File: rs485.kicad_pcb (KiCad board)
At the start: 2 copper layers, 4 parts, among them J1 Conn_01x12_Pin, J3 Conn_01x12_Pin, U2 SN74CB3Q3384APW

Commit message: pcb
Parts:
- moved U2 10.0 mm to (147.3, 92.5)
- moved U1 5.28 mm to (147.4, 82.2)
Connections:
- J1 pad 10: VCC -> Net-(J1-Pin_10)
- J1 pad 12: Net-(J1-Pin_12) -> VCC
- U1 pad 6: Net-(J1-Pin_11) -> Net-(J1-Pin_10)
- U1 pad 7: Net-(J1-Pin_12) -> Net-(J1-Pin_11)
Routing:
- net VCC: track 0.00 -> 30.4 mm
- net Net-(J1-Pin_6): track 0.00 -> 26.7 mm, vias 0 -> 2
- net Net-(J3-Pin_10): track 0.00 -> 22.2 mm, vias 0 -> 2
- net Net-(J3-Pin_12): track 0.00 -> 21.9 mm
- net Net-(J3-Pin_11): track 0.00 -> 20.3 mm, vias 0 -> 2
- net Net-(J1-Pin_1): track 0.00 -> 18.9 mm
- net Net-(J1-Pin_11): track 0.00 -> 18.5 mm
- net Net-(J1-Pin_10): track 0.00 -> 18.0 mm
- net Net-(J1-Pin_5): track 0.00 -> 17.6 mm, vias 0 -> 1
- net GND: track 0.00 -> 17.4 mm
- net Net-(J1-Pin_2): track 0.00 -> 17.0 mm, vias 0 -> 2
- net Net-(J1-Pin_3): track 0.00 -> 16.5 mm, vias 0 -> 2
- net Net-(U1-D): track 0.00 -> 16.3 mm
- net Net-(J1-Pin_4): track 0.00 -> 16.0 mm, vias 0 -> 1
- net Net-(U1-DE): track 0.00 -> 10.4 mm
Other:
- board outline added: 46.2 x 39.9 mm

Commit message: pcb ok.
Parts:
- moved J3 26.5 mm to (133.6, 97.3)
- moved U2 26.2 mm to (150.3, 118.5), turned to 180 degrees
- moved J1 26.2 mm to (165.6, 125.2)
- moved U1 25.7 mm to (150.6, 107.7)
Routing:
- net VCC: track 30.4 -> 67.2 mm
- net Net-(J3-Pin_1): track 0.00 -> 35.7 mm, vias 0 -> 1
- net Net-(J3-Pin_5): track 0.00 -> 34.4 mm
- net Net-(J3-Pin_2): track 0.00 -> 34.1 mm, vias 0 -> 1
- net Net-(J3-Pin_4): track 0.00 -> 30.2 mm
- net Net-(J3-Pin_3): track 0.00 -> 28.8 mm, vias 0 -> 1
- net Net-(J1-Pin_8): track 0.00 -> 20.8 mm
- net Net-(J3-Pin_6): track 0.00 -> 18.6 mm
- net Net-(J3-Pin_7): track 0.00 -> 15.9 mm
- net Net-(J3-Pin_9): track 0.00 -> 15.6 mm, vias 0 -> 1
- net Net-(J1-Pin_7): track 0.00 -> 15.3 mm
- net Net-(J3-Pin_8): track 0.00 -> 15.1 mm
- net Net-(J3-Pin_12): track 21.9 -> 30.7 mm
- net Net-(J1-Pin_4): track 16.0 -> 24.4 mm, vias 1 -> 0
- net Net-(J3-Pin_10): track 22.2 -> 14.2 mm, vias 2 -> 0
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- added copper zone on B.Cu, net GND
- added copper zone on F.Cu, net GND
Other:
- board size 46.2 x 39.9 mm -> 42.2 x 34.8 mm

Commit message: pcb开始制作了。
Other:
- board text added: "10E"
- board text added: "1A3"
- board text added: "1A4"
- board text added: "1A5"
- board text added: "1B1"
- board text added: "1B2"
- board text added: "1B3"
- board text added: "1B4"
- board text added: "1B5"
- board text added: "20E"
- board text added: "2A1"
- board text added: "2A2"
- board text added: "2A3"
- board text added: "2A4"
- board text added: "2A5"
- board text added: "2B1"
- board text added: "2B2"
- board text added: "2B3"
- board text added: "2B4"
- board text added: "2B5"
- board text added: "A"
- board text added: "B"
- board text added: "GND"
- board text added: "VCC"
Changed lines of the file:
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@@
       (plot_on_all_layers_selection 0x0000000_00000000)
       (disableapertmacros false)
-      (usegerberextensions false)
-      (usegerberattributes true)
-      (usegerberadvancedattributes true)
-      (creategerberjobfile true)
+      (usegerberextensions true)
+      (usegerberattributes false)
+      (usegerberadvancedattributes false)
+      (creategerberjobfile false)
       (dashed_line_dash_ratio 12.000000)
       (dashed_line_gap_ratio 3.000000)
@@
       (plotinvisibletext false)
       (sketchpadsonfab false)
-      (subtractmaskfromsilk false)
+      (subtractmaskfromsilk true)
       (outputformat 1)
       (mirror false)
-      (drillshape 1)
+      (drillshape 0)
       (scaleselection 1)
-      (outputdirectory "")
+      (outputdirectory "irg")
     )
   )
@@
   (gr_rect (start 129.286 93.726) (end 171.45 128.524)
     (stroke (width 0.1) (type default)) (fill none) (layer "Edge.Cuts"))
+  (gr_text "1B1" (at 136.144 97.79) (layer "F.SilkS")
+    (effects (font (size 1 1) (thickness 0.15)) (justify left bottom))
+  )
+  (gr_text "VCC" (at 160.274 97.79) (layer "F.SilkS")
+    (effects (font (size 1 1) (thickness 0.15)) (justify left bottom))
+  )
+  (gr_text "2A5" (at 136.906 120.65) (layer "F.SilkS")
+    (effects (font (size 1 1) (thickness 0.15)) (justify left bottom))
+  )
+  (gr_text "2B3" (at 160.274 120.904) (layer "F.SilkS")
+    (effects (font (size 1 1) (thickness 0.15)) (justify left bottom))
+  )
+  (gr_text "1B5" (at 160.274 113.03) (layer "F.SilkS")
+    (effects (font (size 1 1) (thickness 0.15)) (justify left bottom))
+  )
+  (gr_text "2A2" (at 136.144 113.03) (layer "F.SilkS")
+    (effects (font (size 1 1) (thickness 0.15)) (justify left bottom))
+  )
+  (gr_text "1B2" (at 136.144 100.076) (layer "F.SilkS")
+    (effects (font (size 1 1) (thickness 0.15)) (justify left bottom))
+  )
+  (gr_text "1B4" (at 160.274 110.49) (layer "F.SilkS")
+    (effects (font (size 1 1) (thickness 0.15)) (justify left bottom))
+  )
+  (gr_text "10E" (at 136.144 123.444) (layer "F.SilkS")
+    (effects (font (size 1 1) (thickness 0.15)) (justify left bottom))
+  )
+  (gr_text "1A5" (at 136.144 107.95) (layer "F.SilkS")
+    (effects (font (size 1 1) (thickness 0.15)) (justify left bottom))
+  )
+  (gr_text "2A1" (at 136.144 110.744) (layer "F.SilkS")
+    (effects (font (size 1 1) (thickness 0.15)) (justify left bottom))
+  )
+  (gr_text "B" (at 160.274 102.87) (layer "F.SilkS")
+    (effects (font (size 1 1) (thickness 0.15)) (justify left bottom))
+  )
+  (gr_text "2A4" (at 136.144 118.11) (layer "F.SilkS")
+    (effects (font (size 1 1) (thickness 0.15)) (justify left bottom))
+  )
+  (gr_text "1A3" (at 136.144 102.87) (layer "F.SilkS")
+    (effects (font (size 1 1) (thickness 0.15)) (justify left bottom))
+  )
+  (gr_text "2A3" (at 136.144 115.57) (layer "F.SilkS")
+    (effects (font (size 1 1) (thickness 0.15)) (justify left bottom))
+  )
+  (gr_text "GND" (at 160.274 105.41) (layer "F.SilkS")
+    (effects (font (size 1 1) (thickness 0.15)) (justify left bottom))
+  )
+  (gr_text "1A4" (at 136.144 105.41) (layer "F.SilkS")
+    (effects (font (size 1 1) (thickness 0.15)) (justify left bottom))
+  )
+  (gr_text "20E" (at 136.144 125.73) (layer "F.SilkS")
+    (effects (font (size 1 1) (thickness 0.15)) (justify left bottom))
+  )
+  (gr_text "1B3" (at 160.274 107.95) (layer "F.SilkS")
+    (effects (font (size 1 1) (thickness 0.15)) (justify left bottom))
+  )
+  (gr_text "2B5" (at 160.274 125.984) (layer "F.SilkS")
+    (effects (font (size 1 1) (thickness 0.15)) (justify left bottom))
+  )
+  (gr_text "A" (at 160.274 100.33) (layer "F.SilkS")
+    (effects (font (size 1 1) (thickness 0.15)) (justify left bottom))
+  )
+  (gr_text "2B2" (at 160.274 118.11) (layer "F.SilkS")
+    (effects (font (size 1 1) (thickness 0.15)) (justify left bottom))
+  )
+  (gr_text "2B4" (at 160.274 123.952) (layer "F.SilkS")
+    (effects (font (size 1 1) (thickness 0.15)) (justify left bottom))
+  )
+  (gr_text "2B1" (at 160.274 115.57) (layer "F.SilkS")
+    (effects (font (size 1 1) (thickness 0.15)) (justify left bottom))
+  )
   (dimension (type aligned) (layer "F.Fab")
     (pts (xy 171.45 93.726) (xy 171.45 128.524))

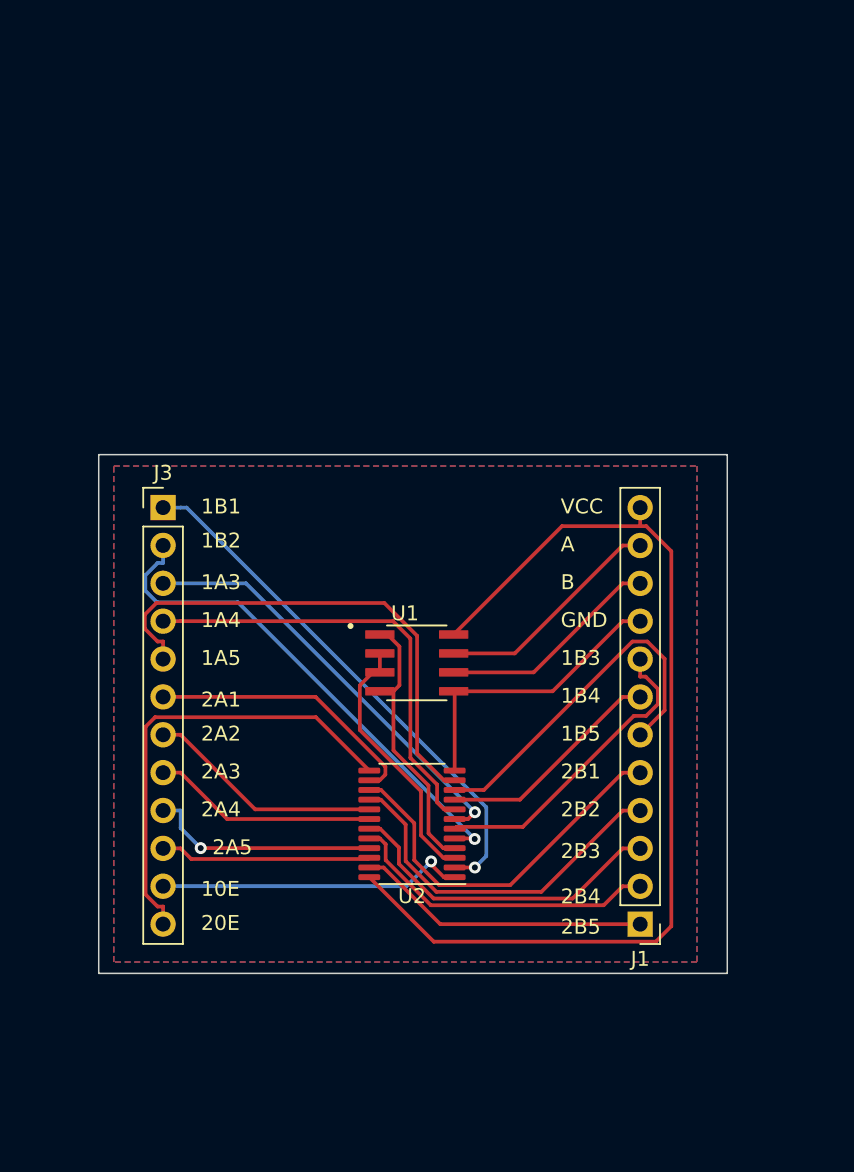
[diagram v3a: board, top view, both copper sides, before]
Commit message: 之前的没问题，现在重新设计，重新制作一个，加电源稳压的电容。
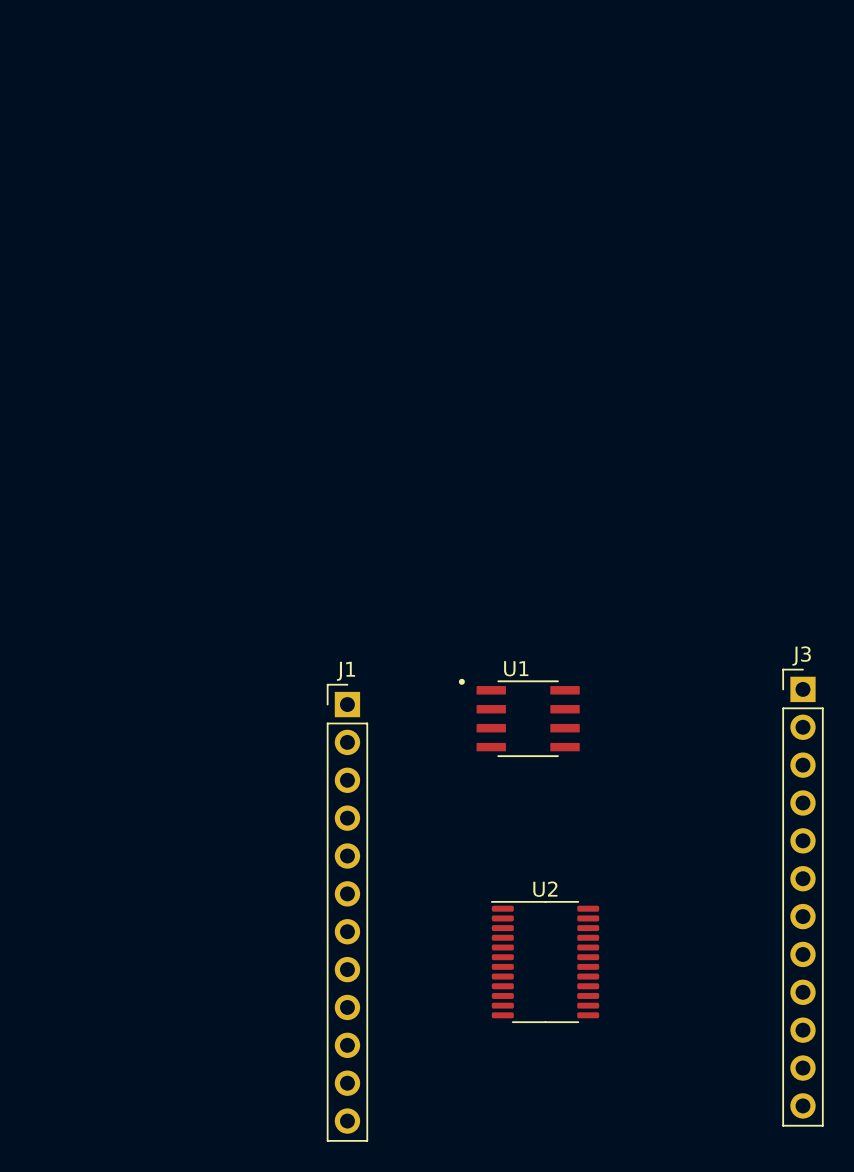
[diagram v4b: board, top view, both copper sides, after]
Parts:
- moved J3 44.6 mm to (176.5, 109.5)
- moved J1 24.5 mm to (146.0, 110.5), turned to 0 degrees
- moved U2 12.9 mm to (159.3, 127.8), turned to 0 degrees
- moved U1 8.36 mm to (158.1, 111.4)
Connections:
- U2 pad 3: Net-(U1-DE) -> Net-(J1-Pin_8)
- U2 pad 4: Net-(U1-D) -> Net-(J3-Pin_2)
- U2 pad 5: Net-(J3-Pin_2) -> Net-(U1-D)
- U2 pad 6: Net-(J1-Pin_8) -> Net-(U1-DE)
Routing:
- net VCC: track 67.2 -> 0.00 mm
- net Net-(J3-Pin_1): track 35.7 -> 0.00 mm, vias 1 -> 0
- net Net-(J3-Pin_5): track 34.4 -> 0.00 mm
- net Net-(J3-Pin_2): track 34.1 -> 0.00 mm, vias 1 -> 0
- net Net-(J3-Pin_12): track 30.7 -> 0.00 mm
- net Net-(J3-Pin_4): track 30.2 -> 0.00 mm
- net Net-(J3-Pin_3): track 28.8 -> 0.00 mm, vias 1 -> 0
- net Net-(J1-Pin_5): track 25.4 -> 0.00 mm
- net Net-(J1-Pin_6): track 24.5 -> 0.00 mm
- net Net-(J1-Pin_4): track 24.4 -> 0.00 mm
- net Net-(J1-Pin_3): track 22.1 -> 0.00 mm
- net Net-(J1-Pin_2): track 21.2 -> 0.00 mm
- net Net-(J1-Pin_8): track 20.8 -> 0.00 mm
- net Net-(J3-Pin_11): track 20.8 -> 0.00 mm, vias 1 -> 0
- net GND: track 19.8 -> 0.00 mm
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- removed copper zone on B.Cu, net GND
- removed copper zone on F.Cu, net GND
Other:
- board outline removed
- board text removed: "10E"
- board text removed: "1A3"
- board text removed: "1A4"
- board text removed: "1A5"
- board text removed: "1B1"
- board text removed: "1B2"
- board text removed: "1B3"
- board text removed: "1B4"
- board text removed: "1B5"
- board text removed: "20E"
- board text removed: "2A1"
- board text removed: "2A2"
- board text removed: "2A3"
- board text removed: "2A4"
- board text removed: "2A5"
- board text removed: "2B1"
- board text removed: "2B2"
- board text removed: "2B3"
- board text removed: "2B4"
- board text removed: "2B5"
- board text removed: "A"
- board text removed: "B"
- board text removed: "GND"
- board text removed: "VCC"
